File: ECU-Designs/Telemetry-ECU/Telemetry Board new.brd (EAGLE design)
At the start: 57.8 x 56.6 mm, 9 parts, among them X1 Suspension Sensor, X2 Wheel Sensor, X3 Tire Temperature Sensor, X5 MINIFIT_5566-4

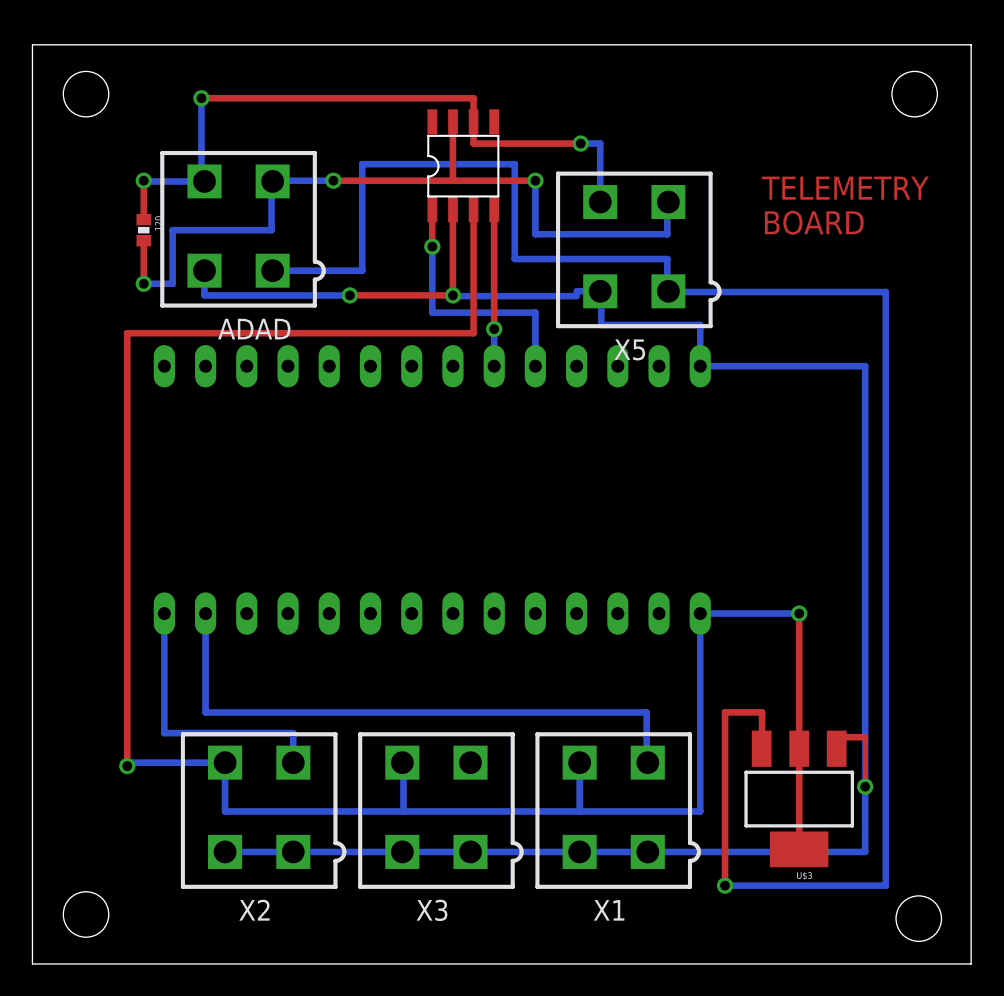
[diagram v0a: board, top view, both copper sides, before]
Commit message: Updated Telemetry Board after Package Problem
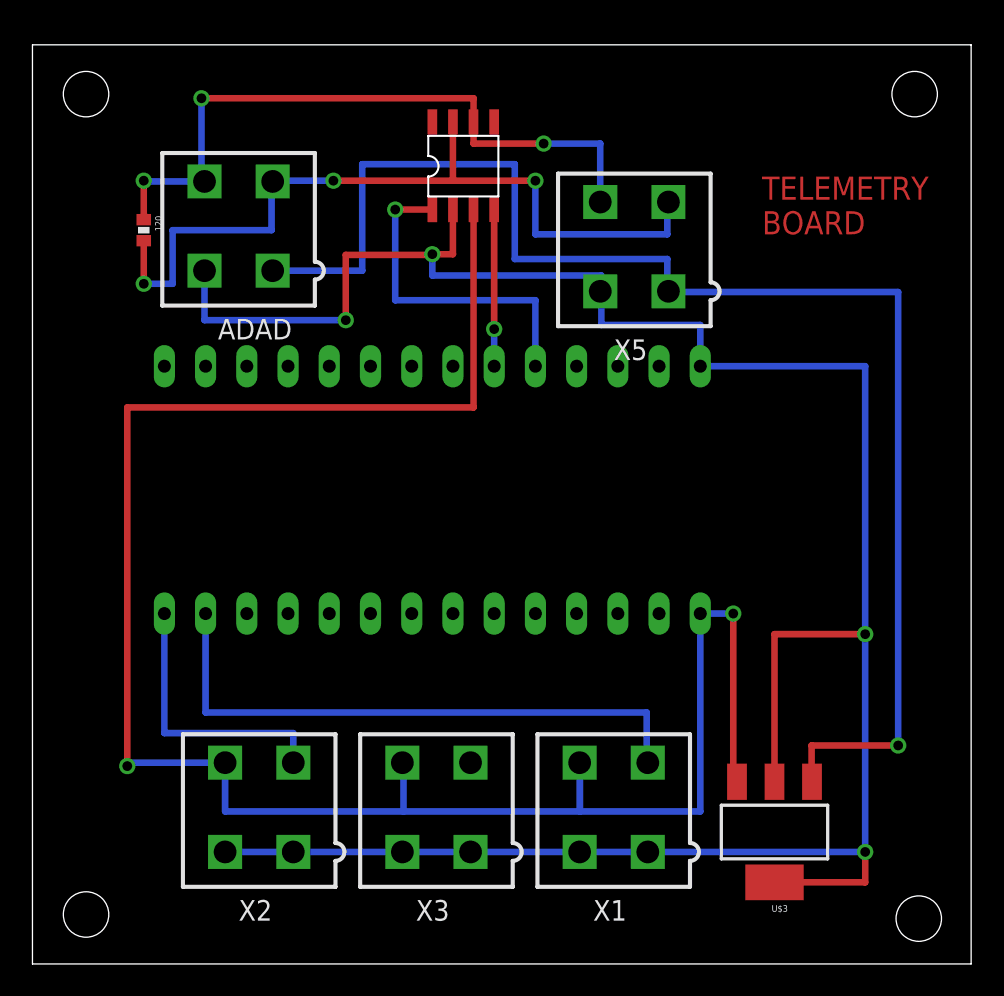
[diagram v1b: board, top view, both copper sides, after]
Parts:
- moved U$3 2.54 mm to (68.8, 8.64)
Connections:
- net N$1: now also U$3.1; no longer U$3.3
- net N$13: now also U$3.3; no longer U$3.2, U$3.4
- net N$6: now also U$3.2, U$3.4; no longer U$3.1
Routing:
- net N$1: track 114.2 -> 88.8 mm
- net N$6: track 127.6 -> 150.3 mm, vias 3 -> 4
- net N$13: track 136.1 -> 128.1 mm
- net N$9: track 16.0 -> 20.6 mm

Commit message: GND MCP2551
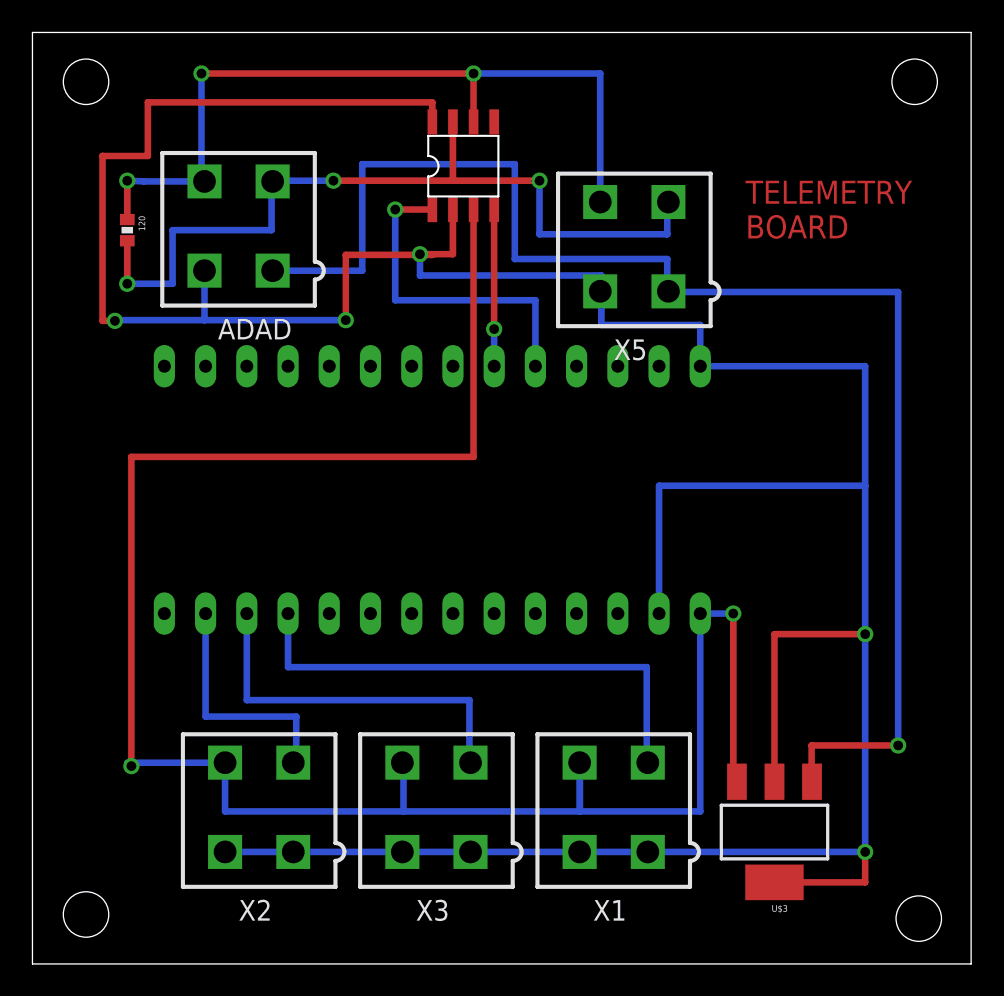
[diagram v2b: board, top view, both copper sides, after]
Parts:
- moved 120 1.02 mm to (29.0, 45.7)
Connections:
- net N$12: now also U$1.A1
- net N$16: now also U$1.A0; no longer U$1.D13
- net N$19: now also U$1.A2; no longer U$1.A0
- net N$6: now also U$1.AGND, U$2.8
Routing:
- net N$6: track 150.3 -> 214.5 mm, vias 4 -> 5
- net N$12: track 0.00 -> 23.0 mm
- net N$4: track 42.3 -> 49.3 mm
- net N$19: track 36.4 -> 31.4 mm
- net N$16: track 17.1 -> 15.0 mm
- net N$3: track 50.4 -> 51.4 mm
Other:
- board size 57.8 x 56.6 mm -> 57.8 x 57.4 mm

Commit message: Compacted Telemetry Board
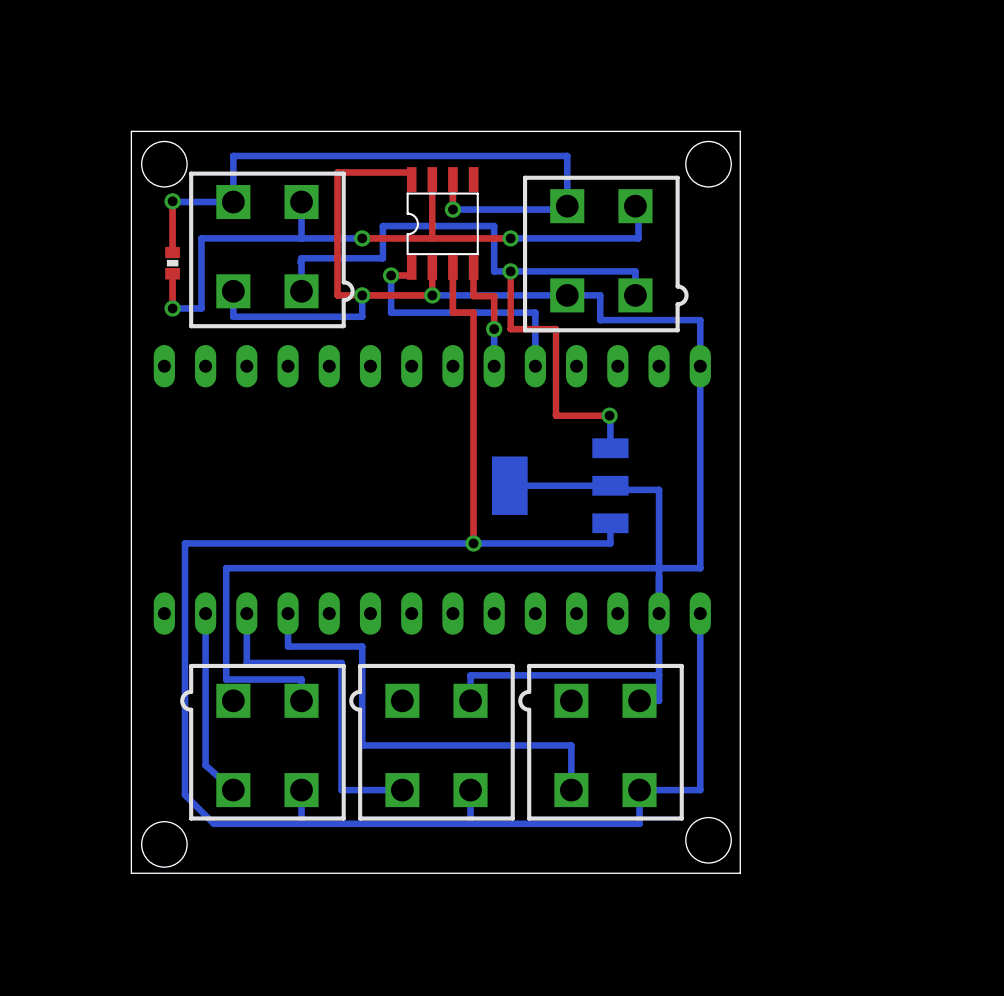
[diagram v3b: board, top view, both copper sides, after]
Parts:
- moved U$3 25.1 mm to (55.6, 30.0), flipped to the bottom, turned to 270 degrees
- moved X1 3.84 mm to (58.4, 14.0), turned to 180 degrees
- moved X2 3.84 mm to (37.6, 14.0), turned to 180 degrees
- moved X3 3.81 mm to (48.0, 14.0), turned to 180 degrees
- moved U$2 3.78 mm to (46.5, 43.4)
- moved 120 3.45 mm to (31.8, 43.7)
- moved ADAD 2.18 mm to (37.6, 44.7)
- moved X5 2.05 mm to (58.2, 44.5)
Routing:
- net N$6: track 214.5 -> 145.4 mm, vias 5 -> 2
- net N$1: track 88.8 -> 46.2 mm, vias 1 -> 2
- net N$13: track 128.0 -> 110.8 mm, vias 2 -> 1
- net N$3: track 51.4 -> 43.2 mm
- net N$4: track 49.3 -> 42.5 mm, vias 3 -> 2
- net N$9: track 20.6 -> 16.3 mm
- net N$16: track 15.0 -> 11.6 mm
- net N$19: track 31.4 -> 28.3 mm
- net N$12: track 23.0 -> 20.5 mm
- net N$10: track 9.65 -> 7.37 mm
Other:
- board size 57.8 x 57.4 mm -> 37.5 x 45.7 mm
- board text removed: "TELEMETRY BOARD"

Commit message: Hopefully the final working of the Telemetry BRD
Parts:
- moved X1 2.29 mm to (58.4, 11.7)
- moved X2 2.29 mm to (37.6, 11.7)
- moved X3 2.29 mm to (48.0, 11.7)
- moved X5 2.03 mm to (60.2, 44.5)
- moved U$1 1.27 mm to (30.0, 37.3)
- moved 120 0.76 mm to (31.0, 43.7)
- moved U$3 0.25 mm to (55.6, 29.7)
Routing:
- net N$13: track 110.8 -> 120.3 mm
- net N$6: track 145.4 -> 153.8 mm
- net N$1: track 46.2 -> 49.0 mm
- net N$3: track 43.2 -> 45.6 mm
- net N$4: track 42.5 -> 44.8 mm
- net N$9: track 16.3 -> 17.5 mm
- net N$10: track 7.37 -> 8.64 mm
- net N$16: track 11.6 -> 12.9 mm
- net N$12: track 20.5 -> 21.5 mm
- net N$19: track 28.3 -> 29.4 mm
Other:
- board size 37.5 x 45.7 mm -> 47.2 x 49.5 mm
